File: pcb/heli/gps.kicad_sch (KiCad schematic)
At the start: 3 parts, among them U4 NEO-M9N-00B

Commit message: 
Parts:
- added J3: CONMHF4-SMD-G-T, LINX_CONMHF4-SMD-G-T, symbol lib:CONMHF4-SMD-G-T
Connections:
- net GND: now also J3.S1, J3.S2, J3.S3
- net at U4.11 (RF_IN): now also J3.1
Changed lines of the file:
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@@
+    (stroke (width 0) (type default) (color 0 0 0 0))
+  )
+  (wire (pts (xy 107.95 66.04) (xy 121.92 66.04))
     (stroke (width 0) (type default) (color 0 0 0 0))
   )
@@
     (pin "2")
   )
+  (symbol (lib_id "lib:CONMHF4-SMD-G-T") (at 105.41 66.04 0) (mirror y) (unit 1)
+    (in_bom yes) (on_board yes) (fields_autoplaced)
+    (property "Reference" "J3" (id 0) (at 100.33 66.2939 0)
+      (effects (font (size 1.27 1.27)) (justify left))
+    )
+    (property "Value" "CONMHF4-SMD-G-T" (id 1) (at 100.33 68.8339 0)
+      (effects (font (size 1.27 1.27)) (justify left))
+    )
+    (property "Footprint" "LINX_CONMHF4-SMD-G-T" (id 2) (at 105.41 66.04 0)
+      (effects (font (size 1.27 1.27)) (justify bottom) hide)
+    )
+    (property "Datasheet" "" (id 3) (at 105.41 66.04 0)
+      (effects (font (size 1.27 1.27)) hide)
+    )
+    (property "PARTREV" "A" (id 4) (at 105.41 66.04 0)
+      (effects (font (size 1.27 1.27)) (justify bottom) hide)
+    )
+    (property "MANUFACTURER" "Linx" (id 5) (at 105.41 66.04 0)
+      (effects (font (size 1.27 1.27)) (justify bottom) hide)
+    )
+    (property "MAXIMUM_PACKAGE_HEIGHT" "0.6 mm" (id 6) (at 105.41 66.04 0)
+      (effects (font (size 1.27 1.27)) (justify bottom) hide)
+    )
+    (property "STANDARD" "Manufacturer Recommendations" (id 7) (at 105.41 66.04 0)
+      (effects (font (size 1.27 1.27)) (justify bottom) hide)
+    )
+    (pin "1")
+    (pin "S1")
+    (pin "S2")
+    (pin "S3")
+  )
   (symbol (lib_id "power:GND") (at 220.98 57.15 0) (unit 1)
     (in_bom yes) (on_board yes) (fields_autoplaced)
@@
       (effects (font (size 1.27 1.27)) hide)
     )
+    (pin "1")
+  )
+  (symbol (lib_id "power:GND") (at 107.95 68.58 90) (mirror x) (unit 1)
+    (in_bom yes) (on_board yes) (fields_autoplaced)
+    (property "Reference" "#PWR04" (id 0) (at 114.3 68.58 0)
+      (effects (font (size 1.27 1.27)) hide)
+    )
+    (property "Value" "GND" (id 1) (at 111.125 68.5799 90)
+      (effects (font (size 1.27 1.27)) (justify right))
+    )
+    (property "Footprint" "" (id 2) (at 107.95 68.58 0)
+      (effects (font (size 1.27 1.27)) hide)
+    )
+    (property "Datasheet" "" (id 3) (at 107.95 68.58 0)
+      (effects (font (size 1.27 1.27)) hide)
+    )

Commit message: 
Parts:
- J3: DIGIKEY (none) -> https://www.digikey.de/en/products/detail/adam-tech/PH1-10-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
- U4: DIGIKEY (none) -> https://www.digikey.de/en/products/detail/u-blox/NEO-M9N-00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
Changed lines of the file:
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@@
       (effects (font (size 1.27 1.27)) (justify bottom) hide)
+    )
+    (property "DIGIKEY" "https://www.digikey.de/en/products/detail/adam-tech/PH1-10-UA/9830653" (id 8) (at 105.41 66.04 0)
+      (effects (font (size 1.27 1.27)) hide)
     )
     (pin "1")
@@
       (effects (font (size 1.27 1.27)) (justify bottom) hide)
     )
+    (property "DIGIKEY" "https://www.digikey.de/en/products/detail/u-blox/NEO-M9N-00B/12149174" (id 8) (at 149.86 78.74 0)
+      (effects (font (size 1.27 1.27)) hide)
+    )
     (pin "1")

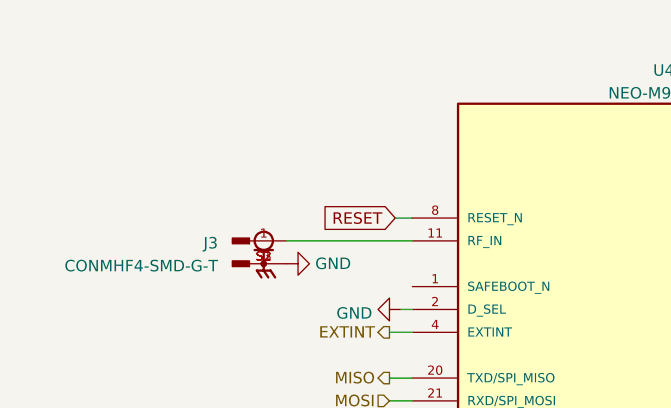
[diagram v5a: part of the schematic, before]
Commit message: 
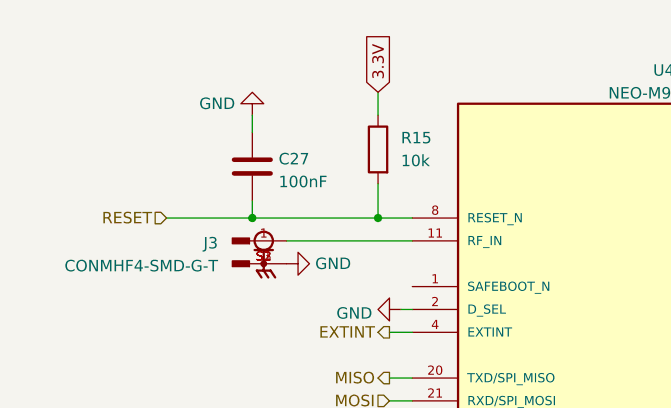
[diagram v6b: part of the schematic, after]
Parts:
- added C27: 100nF, Capacitor_SMD:C_0603_1608Metric, symbol Device:C
- added R15: 10k, Resistor_SMD:R_0603_1608Metric, symbol Device:R
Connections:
- net 3.3V: now also R15.1
- net GND: now also C27.1
- net RESET: now also C27.2, R15.2
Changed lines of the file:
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@@
   (junction (at 187.96 53.34) (diameter 0) (color 0 0 0 0)
   )
+  (junction (at 118.11 63.5) (diameter 0) (color 0 0 0 0)
+  )
+  (junction (at 104.14 63.5) (diameter 0) (color 0 0 0 0)
+  )
   (wire (pts (xy 119.38 91.44) (xy 121.92 91.44))
     (stroke (width 0) (type default) (color 0 0 0 0))
   )
+  (wire (pts (xy 104.14 63.5) (xy 118.11 63.5))
+    (stroke (width 0) (type default) (color 0 0 0 0))
+  )
   (wire (pts (xy 119.38 83.82) (xy 121.92 83.82))
     (stroke (width 0) (type default) (color 0 0 0 0))
@@
     (stroke (width 0) (type default) (color 0 0 0 0))
   )
-  (wire (pts (xy 120.015 63.5) (xy 121.92 63.5))
+  (wire (pts (xy 94.615 63.5) (xy 104.14 63.5))
     (stroke (width 0) (type default) (color 0 0 0 0))
   )
@@
     (stroke (width 0) (type default) (color 0 0 0 0))
   )
+  (wire (pts (xy 104.14 61.595) (xy 104.14 63.5))
+    (stroke (width 0) (type default) (color 0 0 0 0))
+  )
+  (wire (pts (xy 118.11 49.53) (xy 118.11 52.07))
+    (stroke (width 0) (type default) (color 0 0 0 0))
+  )
   (wire (pts (xy 107.95 66.04) (xy 121.92 66.04))
     (stroke (width 0) (type default) (color 0 0 0 0))
   )
+  (wire (pts (xy 118.11 59.69) (xy 118.11 63.5))
+    (stroke (width 0) (type default) (color 0 0 0 0))
+  )
   (wire (pts (xy 178.435 55.88) (xy 177.8 55.88))
     (stroke (width 0) (type default) (color 0 0 0 0))
   )
+  (wire (pts (xy 118.11 63.5) (xy 121.92 63.5))
+    (stroke (width 0) (type default) (color 0 0 0 0))
+  )
   (wire (pts (xy 187.96 58.42) (xy 187.96 53.34))
+    (stroke (width 0) (type default) (color 0 0 0 0))
+  )
+  (wire (pts (xy 104.14 53.975) (xy 104.14 52.07))
     (stroke (width 0) (type default) (color 0 0 0 0))
   )
@@
     )
   )
-  (global_label "RESET" (shape input) (at 120.015 63.5 180) (fields_autoplaced)
-    (effects (font (size 1.27 1.27)) (justify right))
-    (property "Intersheet References" "${INTERSHEET_REFS}" (id 0) (at 111.8567 63.4206 0)
-      (effects (font (size 1.27 1.27)) (justify right) hide)
+  (global_label "3.3V" (shape input) (at 118.11 49.53 90) (fields_autoplaced)
+    (effects (font (size 1.27 1.27)) (justify left))
+    (property "Intersheet References" "${INTERSHEET_REFS}" (id 0) (at 118.0306 43.0045 90)
+      (effects (font (size 1.27 1.27)) (justify left) hide)
     )
   )
@@
     )
   )
+  (hierarchical_label "RESET" (shape input) (at 94.615 63.5 180)
+    (effects (font (size 1.27 1.27)) (justify right))
+  )
   (hierarchical_label "CSN" (shape input) (at 119.38 91.44 180)
     (effects (font (size 1.27 1.27)) (justify right))
@@
       (effects (font (size 1.27 1.27)) (justify bottom) hide)
     )
-    (property "Datasheet" "" (id 3) (at 149.86 78.74 0)
+    (property "Datasheet" "https://content.u-blox.com/sites/default/files/NEO-M9N-00B_DataSheet_UBX-19014285.pdf" (id 3) (at 149.86 78.74 0)
       (effects (font (size 1.27 1.27)) hide)
     )
@@
     (pin "9")
   )
+  (symbol (lib_id "power:GND") (at 104.14 52.07 0) (mirror x) (unit 1)
+    (in_bom yes) (on_board yes) (fields_autoplaced)
+    (property "Reference" "#PWR0119" (id 0) (at 104.14 45.72 0)
+      (effects (font (size 1.27 1.27)) hide)
+    )
+    (property "Value" "GND" (id 1) (at 102.235 50.7999 0)
+      (effects (font (size 1.27 1.27)) (justify right))
+    )
+    (property "Footprint" "" (id 2) (at 104.14 52.07 0)
+      (effects (font (size 1.27 1.27)) hide)
+    )
+    (property "Datasheet" "" (id 3) (at 104.14 52.07 0)
+      (effects (font (size 1.27 1.27)) hide)
+    )
+    (pin "1")
+  )
   (symbol (lib_id "power:GND") (at 178.435 55.88 90) (unit 1)
     (in_bom yes) (on_board yes) (fields_autoplaced)
@@
     (pin "1")
   )
+  (symbol (lib_id "Device:R") (at 118.11 55.88 0) (mirror y) (unit 1)
+    (in_bom yes) (on_board yes) (fields_autoplaced)
+    (property "Reference" "R15" (id 0) (at 120.65 54.6099 0)
+      (effects (font (size 1.27 1.27)) (justify right))
+    )
+    (property "Value" "10k" (id 1) (at 120.65 57.1499 0)
+      (effects (font (size 1.27 1.27)) (justify right))
+    )
+    (property "Footprint" "Resistor_SMD:R_0603_1608Metric" (id 2) (at 119.888 55.88 90)
+      (effects (font (size 1.27 1.27)) hide)
+    )
+    (property "Datasheet" "~" (id 3) (at 118.11 55.88 0)
+      (effects (font (size 1.27 1.27)) hide)
+    )
+    (pin "1")
+    (pin "2")
+  )
   (symbol (lib_id "power:GND") (at 177.8 104.14 90) (unit 1)
     (in_bom yes) (on_board yes) (fields_autoplaced)
@@
     (pin "1")
   )
+  (symbol (lib_id "Device:C") (at 104.14 57.785 0) (unit 1)
+    (in_bom yes) (on_board yes) (fields_autoplaced)
+    (property "Reference" "C27" (id 0) (at 107.061 56.9503 0)
+      (effects (font (size 1.27 1.27)) (justify left))
+    )
+    (property "Value" "100nF" (id 1) (at 107.061 59.4872 0)
+      (effects (font (size 1.27 1.27)) (justify left))
+    )
+    (property "Footprint" "Capacitor_SMD:C_0603_1608Metric" (id 2) (at 105.1052 61.595 0)
+      (effects (font (size 1.27 1.27)) hide)
+    )
+    (property "Datasheet" "~" (id 3) (at 104.14 57.785 0)
+      (effects (font (size 1.27 1.27)) hide)
+    )
+    (pin "1")
+    (pin "2")
+  )
 )

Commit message: 
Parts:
- C25, C26, C27: DIGIKEY (none) -> https://www.digikey.de/en/products/detail/samsung-electro-m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
- R15: DIGIKEY (none) -> https://www.digikey.de/en/products/detail/walsin-technology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
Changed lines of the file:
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@@
+      (effects (font (size 1.27 1.27)) hide)
+    )
+    (property "DIGIKEY" "https://www.digikey.de/en/products/detail/samsung-electro-mechanics/CL10B104KB8NNWC/3887593" (id 4) (at 232.41 53.34 0)
       (effects (font (size 1.27 1.27)) hide)
     )
@@
     )
     (property "Datasheet" "~" (id 3) (at 220.98 53.34 0)
+      (effects (font (size 1.27 1.27)) hide)
+    )
+    (property "DIGIKEY" "https://www.digikey.de/en/products/detail/samsung-electro-mechanics/CL10B104KB8NNWC/3887593" (id 4) (at 220.98 53.34 0)
       (effects (font (size 1.27 1.27)) hide)
     )
@@
       (effects (font (size 1.27 1.27)) hide)
     )
+    (property "DIGIKEY" "https://www.digikey.de/en/products/detail/walsin-technology-corporation/WR06X103-JTL/13239132" (id 4) (at 118.11 55.88 0)
+      (effects (font (size 1.27 1.27)) hide)
+    )
     (pin "1")
     (pin "2")
@@
       (effects (font (size 1.27 1.27)) hide)
     )
+    (property "DIGIKEY" "https://www.digikey.de/en/products/detail/samsung-electro-mechanics/CL10B104KB8NNWC/3887593" (id 4) (at 104.14 57.785 0)
+      (effects (font (size 1.27 1.27)) hide)
+    )

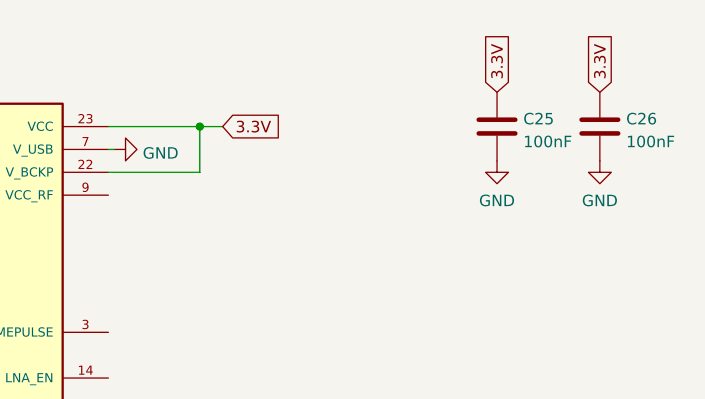
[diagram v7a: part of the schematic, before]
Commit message: 
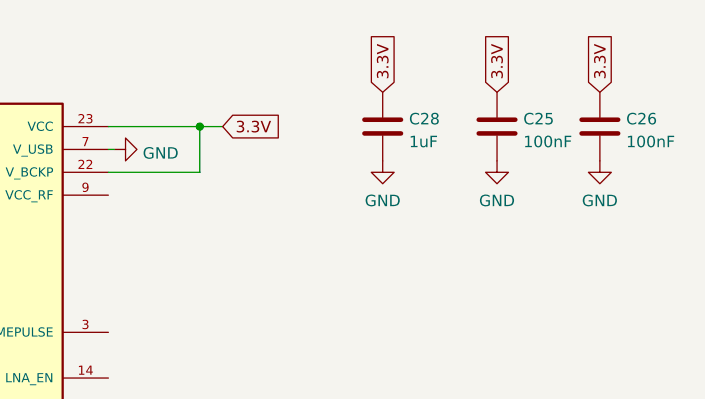
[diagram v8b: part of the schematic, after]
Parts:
- added C28: 1uF, Capacitor_SMD:CP_Elec_4x5.4, symbol Device:C
- C25, C26, C27: DIGIKEY https://www.digikey.de/en/products/detail/samsung-electro-m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 -> 1276-1935-1-ND
- J3: DIGIKEY https://www.digikey.de/en/products/detail/adam-tech/PH1-10-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 -> 2057-PH1-10-UA-ND
- R15: DIGIKEY https://www.digikey.de/en/products/detail/walsin-technology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 -> 1292-WR06X103JTLCT-ND
- U4: DIGIKEY https://www.digikey.de/en/products/detail/u-blox/NEO-M9N-00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 -> 672-NEO-M9N-00BCT-ND
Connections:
- net 3.3V: now also C28.1
- net GND: now also C28.2
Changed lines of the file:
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@@
+    )
+  )
+  (global_label "3.3V" (shape input) (at 208.28 49.53 90) (fields_autoplaced)
+    (effects (font (size 1.27 1.27)) (justify left))
+    (property "Intersheet References" "${INTERSHEET_REFS}" (id 0) (at 208.2006 43.0045 90)
+      (effects (font (size 1.27 1.27)) (justify left) hide)
     )
   )
@@
       (effects (font (size 1.27 1.27)) hide)
     )
-    (property "DIGIKEY" "https://www.digikey.de/en/products/detail/samsung-electro-mechanics/CL10B104KB8NNWC/3887593" (id 4) (at 232.41 53.34 0)
+    (property "DIGIKEY" "1276-1935-1-ND" (id 4) (at 232.41 53.34 0)
       (effects (font (size 1.27 1.27)) hide)
     )
@@
       (effects (font (size 1.27 1.27)) (justify bottom) hide)
     )
-    (property "DIGIKEY" "https://www.digikey.de/en/products/detail/adam-tech/PH1-10-UA/9830653" (id 8) (at 105.41 66.04 0)
+    (property "DIGIKEY" "2057-PH1-10-UA-ND" (id 8) (at 105.41 66.04 0)
       (effects (font (size 1.27 1.27)) hide)
     )
@@
       (effects (font (size 1.27 1.27)) hide)
     )
-    (property "DIGIKEY" "https://www.digikey.de/en/products/detail/samsung-electro-mechanics/CL10B104KB8NNWC/3887593" (id 4) (at 220.98 53.34 0)
+    (property "DIGIKEY" "1276-1935-1-ND" (id 4) (at 220.98 53.34 0)
+      (effects (font (size 1.27 1.27)) hide)
+    )
+    (pin "1")
+    (pin "2")
+  )
+  (symbol (lib_id "Device:C") (at 208.28 53.34 0) (unit 1)
+    (in_bom yes) (on_board yes) (fields_autoplaced)
+    (property "Reference" "C28" (id 0) (at 211.201 52.5053 0)
+      (effects (font (size 1.27 1.27)) (justify left))
+    )
+    (property "Value" "1uF" (id 1) (at 211.201 55.0422 0)
+      (effects (font (size 1.27 1.27)) (justify left))
+    )
+    (property "Footprint" "Capacitor_SMD:CP_Elec_4x5.4" (id 2) (at 209.2452 57.15 0)
+      (effects (font (size 1.27 1.27)) hide)
+    )
+    (property "Datasheet" "~" (id 3) (at 208.28 53.34 0)
+      (effects (font (size 1.27 1.27)) hide)
+    )
+    (property "DIGIKEY" "1276-1935-1-ND" (id 4) (at 208.28 53.34 0)
       (effects (font (size 1.27 1.27)) hide)
     )
@@
       (effects (font (size 1.27 1.27)) (justify bottom) hide)
     )
-    (property "DIGIKEY" "https://www.digikey.de/en/products/detail/u-blox/NEO-M9N-00B/12149174" (id 8) (at 149.86 78.74 0)
+    (property "DIGIKEY" "672-NEO-M9N-00BCT-ND" (id 8) (at 149.86 78.74 0)
       (effects (font (size 1.27 1.27)) hide)
     )
@@
       (effects (font (size 1.27 1.27)) hide)
     )
-    (property "DIGIKEY" "https://www.digikey.de/en/products/detail/walsin-technology-corporation/WR06X103-JTL/13239132" (id 4) (at 118.11 55.88 0)
-      (effects (font (size 1.27 1.27)) hide)
-    )
-    (pin "1")
-    (pin "2")
+    (property "DIGIKEY" "1292-WR06X103JTLCT-ND" (id 4) (at 118.11 55.88 0)
+      (effects (font (size 1.27 1.27)) hide)
+    )
+    (pin "1")
+    (pin "2")
+  )
+  (symbol (lib_id "power:GND") (at 208.28 57.15 0) (unit 1)
+    (in_bom yes) (on_board yes) (fields_autoplaced)
+    (property "Reference" "#PWR032" (id 0) (at 208.28 63.5 0)
+      (effects (font (size 1.27 1.27)) hide)
+    )
+    (property "Value" "GND" (id 1) (at 208.28 61.5934 0))
+    (property "Footprint" "" (id 2) (at 208.28 57.15 0)
+      (effects (font (size 1.27 1.27)) hide)
+    )
+    (property "Datasheet" "" (id 3) (at 208.28 57.15 0)
+      (effects (font (size 1.27 1.27)) hide)
+    )
+    (pin "1")
   )
   (symbol (lib_id "power:GND") (at 177.8 104.14 90) (unit 1)
@@
       (effects (font (size 1.27 1.27)) hide)
     )
-    (property "DIGIKEY" "https://www.digikey.de/en/products/detail/samsung-electro-mechanics/CL10B104KB8NNWC/3887593" (id 4) (at 104.14 57.785 0)
-      (effects (font (size 1.27 1.27)) hide)
-    )
+    (property "DIGIKEY" "1276-1935-1-ND" (id 4) (at 104.14 57.785 0)
+      (effects (font (size 1.27 1.27)) hide)
+    )
